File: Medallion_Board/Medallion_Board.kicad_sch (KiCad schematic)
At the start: 79 parts, among them J1 RYLR998, J2 EXPANSION, P1 JST_PH, P2 JST_BTN_1, P3 JST_BTN_2, P4 JST_BTN_3, P5 JST_EN, Q1 DMG3415U, SW1 KMR2, SW2 KMR2, U1 RT9080-33GJ5, U2 LC86LICMD, U3 ESP32-S3-MINI-1-N8, U4 BNO085, U5 MAX17048G_T10, U6 MCP73831T-2ACI_OT, X1 USB4085-GF-A

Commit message: migrating to nRF controller
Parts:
- removed C14, C18, C3: 1uF, Capacitor_SMD:C_0603_1608Metric, symbol Adafruit ESP32-S3 8MB No PSRAM-eagle-import:CAP_CERAMIC0603_NO
- removed C6: 10uF, Capacitor_SMD:C_0805_2012Metric, symbol Adafruit ESP32-S3 8MB No PSRAM-eagle-import:CAP_CERAMIC0805-NOOUTLINE
- removed C7: 0.1uF, Capacitor_SMD:C_0402_1005Metric, symbol Adafruit ESP32-S3 8MB No PSRAM-eagle-import:CAP_CERAMIC0805-NOOUTLINE
- removed C8: 47pF, Capacitor_SMD:C_0402_1005Metric, symbol Adafruit ESP32-S3 8MB No PSRAM-eagle-import:CAP_CERAMIC0805-NOOUTLINE
- removed FL1, FL2: BLM15EG121SN1D, BLM15EG121SN1D:BEADC1005X55N, symbol BLM15EG121SN1D:BLM15EG121SN1D
- removed J1: RYLR998, Connector_PinHeader_2.54mm:RYLR998, symbol Connector_Generic:Conn_01x05
- removed P5: JST_EN, S2B-PH-SM4-TB_LF__SN_:JST_S2B-PH-SM4-TB_LF__SN_, symbol S2B-PH-SM4-TB_LF__SN_:S2B-PH-SM4-TB_LF__SN_
- removed R2: 100K, Resistor_SMD:R_0603_1608Metric, symbol Adafruit ESP32-S3 8MB No PSRAM-eagle-import:RESISTOR_0603_NOOUT
- removed SW2: KMR2, Button_Switch_SMD:SW_Push_1P1T-SH_NO_CK_KMR2xxG, symbol Adafruit ESP32-S3 8MB No PSRAM-eagle-import:SWITCH_TACT_SMT4.6X2.8
- removed U3: ESP32-S3-MINI-1-N8, ESP32-S3-MINI-1-N8:XCVR_ESP32-S3-MINI-1-N8, symbol ESP32-S3-MINI-1-N8:ESP32-S3-MINI-1-N8
- added C3, C4: 10uF, Capacitor_SMD:C_0805_2012Metric, symbol Adafruit ESP32-S3 8MB No PSRAM-eagle-import:CAP_CERAMIC0805-NOOUTLINE
- added C6: 1uF, Capacitor_SMD:C_0603_1608Metric, symbol Adafruit ESP32-S3 8MB No PSRAM-eagle-import:CAP_CERAMIC0603_NO
- added L1: 10uH, LQM18DN100M70L:INDC1608X95N, symbol LQM18DN100M70L:LQM18DN100M70L
- added P1: JST_ONOFF, S2B-PH-SM4-TB_LF__SN_:JST_S2B-PH-SM4-TB_LF__SN_, symbol S2B-PH-SM4-TB_LF__SN_:S2B-PH-SM4-TB_LF__SN_
- added R1: 5.1K, Resistor_SMD:R_0603_1608Metric, symbol Adafruit ESP32-S3 8MB No PSRAM-eagle-import:RESISTOR_0603_NOOUT
- added R10, R11: 1K, Resistor_SMD:R_0603_1608Metric, symbol Adafruit ESP32-S3 8MB No PSRAM-eagle-import:RESISTOR_0603_NOOUT
- added R19, R21: 27R, Resistor_SMD:R_0603_1608Metric, symbol Adafruit ESP32-S3 8MB No PSRAM-eagle-import:RESISTOR_0603_NOOUT
- added U1: MDBT50Q-1MV2, MDBT50Q-1MV2:XCVR_MDBT50Q-1MV2, symbol MDBT50Q-1MV2:MDBT50Q-1MV2
- added Y1: 32.768KHZ, ABS07-32.768KHZ-7-T:XTAL_ABS07-32.768KHZ-7-T, symbol ABS07-32.768KHZ-7-T:ABS07-32.768KHZ-7-T
- C1, C2: value 10uF -> 12pF; footprint Capacitor_SMD:C_0805_2012Metric -> Capacitor_SMD:C_0402_1005Metric
- C8: renamed from C4; value KW-5R5C104-R -> 100mF
- D10, D11, D3, D4, D5, D6, D7, D8, D9: MPN (none) -> WS2812B-2020
- P2: renamed from P1; MPN (none) -> S2B-PH-SM4-TB(LF)(SN); PRICE (none) -> 0.37
- P3: renamed from P2; MPN (none) -> S2B-PH-SM4-TB(LF)(SN); PRICE (none) -> 0.37
- P4: MPN (none) -> S2B-PH-SM4-TB(LF)(SN); PRICE (none) -> 0.37
- P5: renamed from P3; MPN (none) -> S2B-PH-SM4-TB(LF)(SN); PRICE (none) -> 0.37
- R4: value 1Meg -> 100K
- R7: value 5.1K -> 5.6K
- renumbered C12 to C10, C10 to C11, C11 to C12, C21 to C13, C13 to C14, C22 to C15, C23 to C16, C24 to C17, C25 to C18, C26 to C19, C27 to C20, C28 to C21, C29 to C22, C30 to C23, C15 to C24, C17 to C25, C31 to C26, C16 to C27, C20 to C28, C19 to C7, J2 to J1, R8 to R12, R10 to R13, R16 to R14, R17 to R15, R9 to R16, R5 to R17, R6 to R18, R11 to R2, R13 to R20, R12 to R3, R1 to R5, R14 to R6, R15 to R8, R3 to R9, U5 to U2, U2 to U3, U1 to U4, U6 to U5, U4 to U6
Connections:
- net IO34_DBLTAP is gone; now on an unnamed net: R4.2
- net TXD0 is gone; now on an unnamed net: U3.1 (RXD)
- net 3.3V: now also R12.2, R13.2, R16.2, R2.2, R3.2, C4.1, R1.2, U1.30 (VDDH); no longer C1.1, C2.1, R7.2
- net BNO_NINT: now also U1.25 (P1.08)
- net BNO_NRST: now also U1.26 (P1.09/TRACEDATA3)
- net D+: now also R19.1, U1.35 (D+); no longer X1.A6 (DP1)
- net D-: now also R21.1, U1.34 (D-); no longer X1.B6 (DP2)
- net GND: now also C1.1, C2.1, R7.2, U6.10 (CLKSEL0), C3.2, C4.2, C6.2, P1.2, U1.1 (GND), U1.15 (GND), U1.2 (GND), U1.33 (GND), U1.55 (GND); no longer C1.2, C2.2, R4.1
- net GPS_ANT_ACTIVE: now also U1.7 (P1.14)
- net GPS_RESET: now also U1.8 (P1.15)
- net GPS_WAKEUP: now also U1.6 (P1.13)
- net LOW_BATT: now also U1.57 (P1.06)
- net NEOPIX: now also U1.58 (P1.07)
- net SCL: now also U1.16 (P0.27)
- net SDA: now also U1.19 (P0.26)
- net STATUS_LED: now also U1.59 (P1.05)
- net USER_BTN_1: now also U1.3 (P1.10)
- net USER_BTN_2: now also U1.4 (P1.11)
- net USER_BTN_3: now also U1.5 (P1.12)
- net VBUS: now also C5.1, U1.32 (VBUS)
- net VHI: now also R4.1
- net at U4.3 (EN): now also P1.1
- net OSC2: now reaches U6.26 (XOUT32/CLKSEL1)
- net OSC2: now also C2.2, U1.18 (P0.01/XL2), Y1.1
- net OSC1: now reaches U6.27 (XIN32)
- net OSC1: now also C1.2, U1.17 (P0.00/XL1), Y1.2
- removed net +3.3V: C5.1, R12.2, R13.2, R16.2, R2.2, R3.2
- net GPIO01 renamed GPIO19
- net GPIO19: now also U1.42 (P0.19)
- net GPIO02 renamed GPIO20
- net GPIO20: now also U1.44 (P0.20)
- net GPIO06 renamed GPIO21
- net GPIO21: now also U1.43 (P0.21)
- net GPIO11 renamed GPIO22
- net GPIO22: now also U1.46 (P0.22)
- net RESET: no longer names the net of R7.1
- net RESET: now also R10.2; no longer SW1.2
- net RXD0: no longer names the net of U3.2 (TXD)
- net RXD0: now also R11.1
- new net: C3.1, L1.2, U1.28 (VDD)
- new net: L1.1, U1.31 (DCCH)
- new net: R19.2, X1.A6 (DP1)
- new net: R21.2, X1.B6 (DP2)
- new net RXD_GPS: R11.2, U1.24 (P0.08)
- new net TXD_GPS: R10.1, U1.22 (P0.06)
- new net uC_RESET: C6.1, R1.1, SW1.2, U1.40 (P0.18/~{RESET})
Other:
- note added: "GNSS"
- note added: "LED"
- note added: "USB"
- note added: "nRF MODULE"
- note removed: "Bulk decoupling"
- note removed: "CONTROLLER"
- note removed: "GPS"
- note removed: "High-frequency filter"
- note removed: "I2C SUPPORT"
- note removed: "NEOPIXEL"
- note removed: "Place as near to ESP32 power rail as possible"
- note removed: "USB AND PROGRAMMING BUTTONS"
- moved on the sheet: C10, C11, C12, C13, C14, C15, C16, C17, C18, C19, C20, C21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

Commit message: Migrate to the nRF microcontroller. Attempt to implement my own lora section - will probably remove later.
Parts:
- added C28: 4.7uF, Capacitor_SMD:C_0603_1608Metric, symbol Adafruit ESP32-S3 8MB No PSRAM-eagle-import:CAP_CERAMIC0603_NO
- added C30, C31: NC, Capacitor_SMD:C_0603_1608Metric, symbol Adafruit ESP32-S3 8MB No PSRAM-eagle-import:CAP_CERAMIC0603_NO
- added IC1: 114993121, Wio-E5-LE:114993121, symbol 114993121:114993121
- added J2: RECE.20369.001E.01, RECE.20369:RECE20369001E01, symbol RECE_20369_001E_01:RECE.20369.001E.01
- added L2: 0R, LQM18DN100M70L:INDC1608X95N, symbol LQM18DN100M70L:LQM18DN100M70L
- added R17: 470R, Resistor_SMD:R_0603_1608Metric, symbol Adafruit ESP32-S3 8MB No PSRAM-eagle-import:RESISTOR_0603_NOOUT
- added R23: 5.6K, Resistor_SMD:R_0603_1608Metric, symbol Adafruit ESP32-S3 8MB No PSRAM-eagle-import:RESISTOR_0603_NOOUT
- added R24, R25: 22R, Resistor_SMD:R_0603_1608Metric, symbol Adafruit ESP32-S3 8MB No PSRAM-eagle-import:RESISTOR_0603_NOOUT
- added SW2: KMR2, Button_Switch_SMD:SW_Push_1P1T-SH_NO_CK_KMR2xxG, symbol Adafruit ESP32-S3 8MB No PSRAM-eagle-import:SWITCH_TACT_SMT4.6X2.8
- renumbered C28 to C29, R17 to R18, R18 to R19, R19 to R20, R20 to R21, R21 to R22
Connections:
- net 3.3V: now also C28.1, IC1.1 (VCC)
- net GND: now also C28.2, C30.2, C31.2, IC1.14 (GND_2), IC1.16 (GND_3), IC1.2 (GND_1), IC1.22 (GND_4), J2.1 (GND_1), J2.2 (GND_2), J2.3 (GND_3), R17.2, R23.2
- net RXD_LORA: now reaches U1.36 (P0.14)
- net RXD_LORA: now also R25.2
- net TXD_LORA: now reaches U1.37 (P0.13)
- net TXD_LORA: now also R24.1
- net LORA_RST: now reaches U1.56 (P1.04)
- net LORA_RST: now also IC1.17 (RST)
- new net: C30.1, IC1.15 (RFIO), L2.1
- new net: IC1.9 (PB7), R23.1, R24.2
- new net: IC1.10 (PB6), R25.1
- new net: IC1.24 (PB13), SW2.1
- new net: R17.1, SW2.2
- new net: C31.1, J2.4 (CENTRE), L2.2
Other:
- note added: "I need to figure out the values for the inductor and capacitors."
- title: (none) -> Off-grid People Tracking Puck

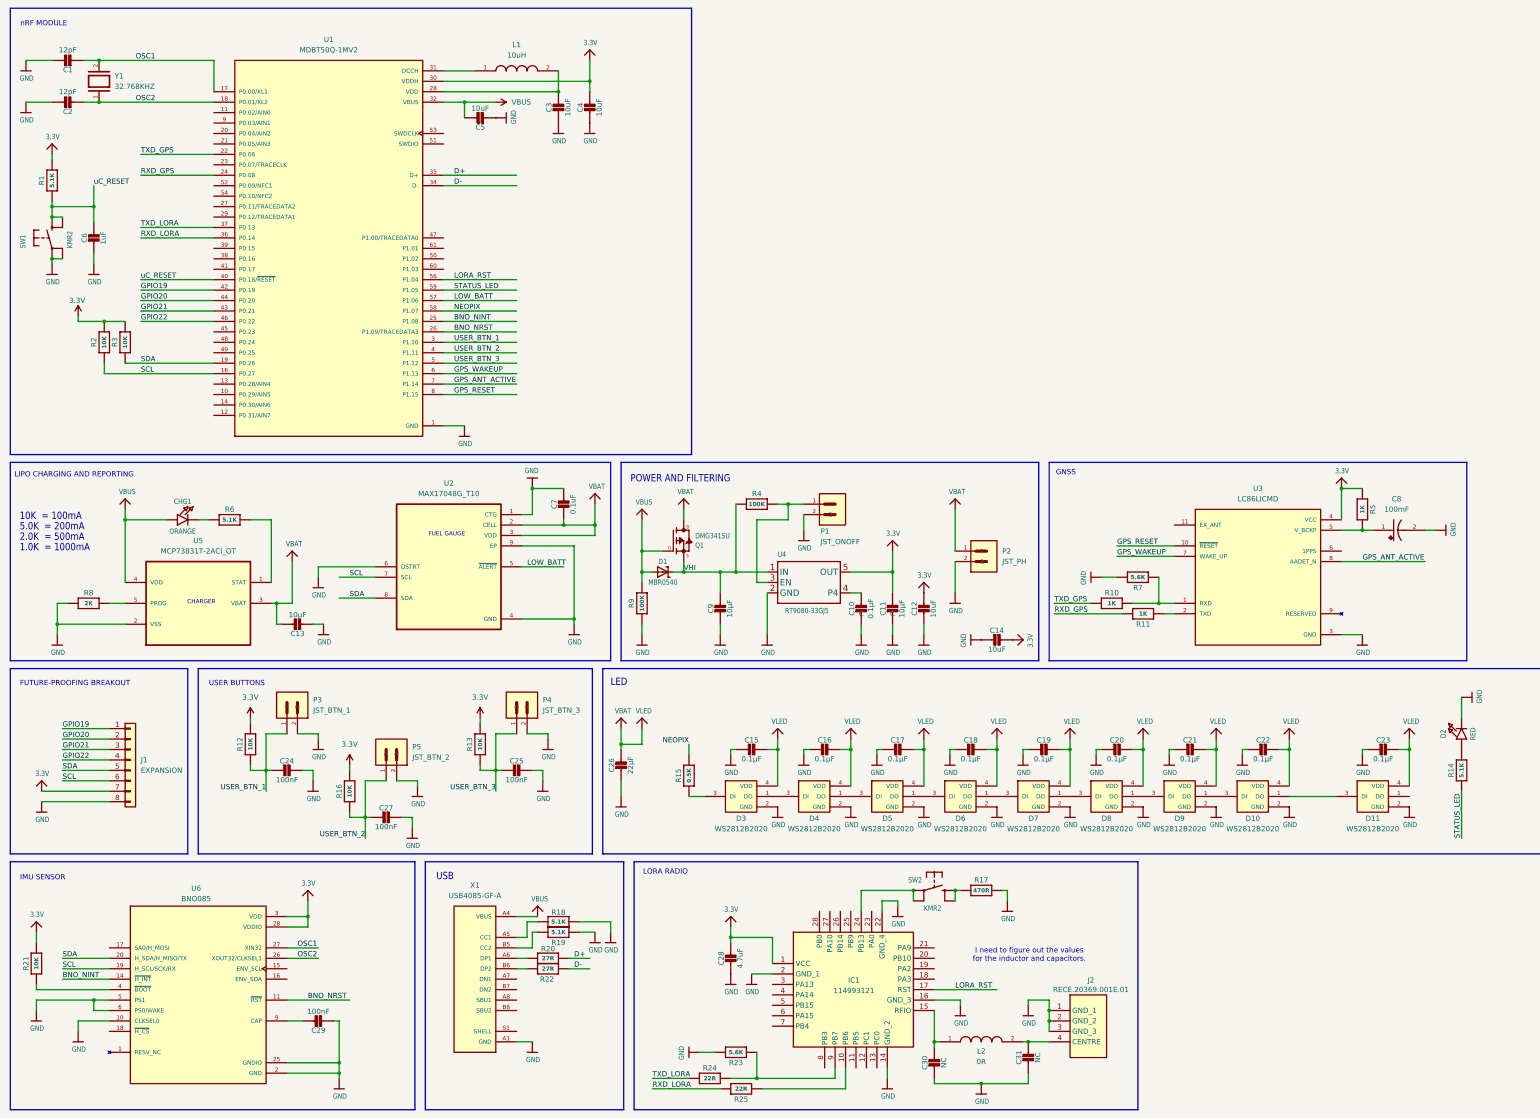
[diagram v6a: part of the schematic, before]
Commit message: Start PCB design again - compact requirements
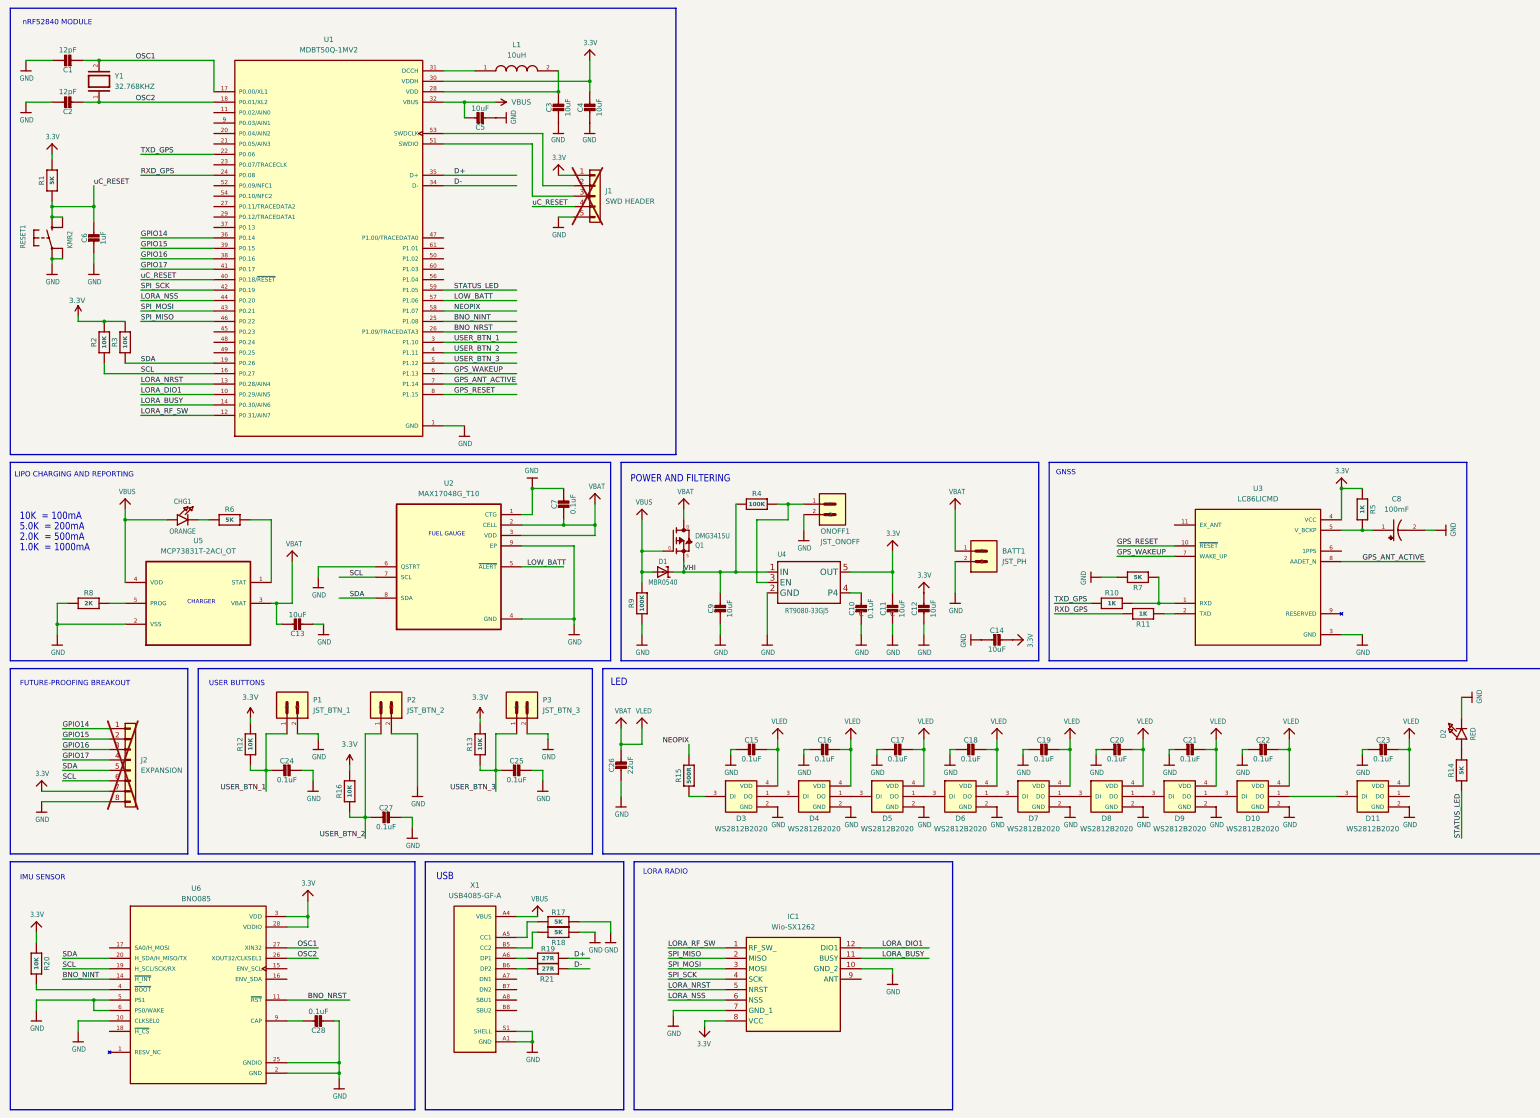
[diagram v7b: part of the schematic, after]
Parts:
- removed C28: 4.7uF, Capacitor_SMD:C_0603_1608Metric, symbol Adafruit ESP32-S3 8MB No PSRAM-eagle-import:CAP_CERAMIC0603_NO
- removed C30, C31: NC, Capacitor_SMD:C_0603_1608Metric, symbol Adafruit ESP32-S3 8MB No PSRAM-eagle-import:CAP_CERAMIC0603_NO
- removed IC1: 114993121, Wio-E5-LE:114993121, symbol 114993121:114993121
- removed J2: RECE.20369.001E.01, RECE.20369:RECE20369001E01, symbol RECE_20369_001E_01:RECE.20369.001E.01
- removed L2: 0R, LQM18DN100M70L:INDC1608X95N, symbol LQM18DN100M70L:LQM18DN100M70L
- removed R17: 470R, Resistor_SMD:R_0603_1608Metric, symbol Adafruit ESP32-S3 8MB No PSRAM-eagle-import:RESISTOR_0603_NOOUT
- removed R23: 5.6K, Resistor_SMD:R_0603_1608Metric, symbol Adafruit ESP32-S3 8MB No PSRAM-eagle-import:RESISTOR_0603_NOOUT
- removed R24, R25: 22R, Resistor_SMD:R_0603_1608Metric, symbol Adafruit ESP32-S3 8MB No PSRAM-eagle-import:RESISTOR_0603_NOOUT
- removed SW2: KMR2, Button_Switch_SMD:SW_Push_1P1T-SH_NO_CK_KMR2xxG, symbol Adafruit ESP32-S3 8MB No PSRAM-eagle-import:SWITCH_TACT_SMT4.6X2.8
- added IC1: Wio-SX1262, 114993390:114993390, symbol 114993390:114993390
- added J1: SWD HEADER, Connector_PinHeader_2.54mm:PinHeader_1x05_P2.54mm_Vertical, symbol Connector_Generic:Conn_01x05
- C1, C2: MPN (none) -> GMC04CG120J6R3NT
- C10: value 0.1µF -> 0.1uF; MPN (none) -> 0402B104K160HI
- C11, C13, C9: value 10µF -> 10uF; MPN (none) -> 0805W106K6R3CC
- C12, C14, C3, C4, C5: MPN (none) -> 0805W106K6R3CC
- C15, C16, C17, C18, C19, C20, C21, C22, C23: value 0.1µF -> 0.1uF; footprint Capacitor_SMD:C_0603_1608Metric -> Capacitor_SMD:C_0402_1005Metric; MPN (none) -> 0402B104K160HI
- C24, C25, C27: value 100nF -> 0.1uF; footprint Capacitor_SMD:C_0603_1608Metric -> Capacitor_SMD:C_0402_1005Metric; MPN (none) -> 0402B104K160HI
- C26: value 22µF -> 22uF; footprint Capacitor_SMD:C_0805_2012Metric -> Capacitor_SMD:C_0402_1005Metric; MPN (none) -> GRM155R61A224KE19D
- C28: renamed from C29; value 100nF -> 0.1uF; footprint Capacitor_SMD:C_0603_1608Metric -> Capacitor_SMD:C_0402_1005Metric; MPN (none) -> 0402B104K160HI
- C6: MPN (none) -> 0603B105K100XD
- C7: MPN (none) -> 0402B104K160HI
- C8: MANUFACTURER Seiko -> (none); MF Seiko Instruments -> (none); MP XH414HG-IV01E -> (none)
- CHG1: footprint LED_SMD:LED_0805_2012Metric -> LED_SMD:LED_0603_1608Metric
- J2: renamed from J1; now not fitted
- R1, R14, R6: value 5.1K -> 5K; MPN (none) -> RT0603BRE075KL
- R10, R11, R5: MPN (none) -> RC0603FR-071KL
- R12, R13, R16, R2, R3: MPN (none) -> RC0603FR-0710KL
- R15: value 0.5K -> 500R; MPN (none) -> RT0603BRC07500RL
- R17: renamed from R18; value 5.1K -> 5K; MPN (none) -> RT0603BRE075KL
- R18: renamed from R19; value 5.1K -> 5K; MPN (none) -> RT0603BRE075KL
- R19: renamed from R20; MPN (none) -> RC0603FR-0727RL
- R20: renamed from R21; MPN (none) -> RC0603FR-0710KL
- R21: renamed from R22; MPN (none) -> RC0603FR-0727RL
- R4, R9: MPN (none) -> RC0603FR-07100KL
- R7: value 5.6K -> 5K; MPN (none) -> RT0603BRE075KL
- R8: MPN (none) -> RC0603FR-072KL
- renumbered P2 to BATT1, P1 to ONOFF1, P3 to P1, P5 to P2, P4 to P3, SW1 to RESET1
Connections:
- net RXD_LORA is gone; now on net GPIO14: U1.36 (P0.14)
- net 3.3V: now also IC1.8 (VCC), J1.1 (VCC)
- net GND: now also X1.S1 (SHELL), X1.S2 (SHELL), X1.S3 (SHELL), X1.S4 (SHELL), IC1.10 (GND_2), IC1.7 (GND_1), J1.5 (GND)
- net uC_RESET: now also J1.4 (RST)
- net LORA_DIO1: now reaches U1.10 (P0.29/AIN5)
- net LORA_DIO1: now also IC1.12 (DIO1)
- net LORA_RF_SW: now reaches U1.12 (P0.31/AIN7)
- net LORA_RF_SW: now also IC1.1 (RF_SW_)
- net LORA_NRST: now reaches U1.13 (P0.28/AIN4)
- net LORA_NRST: now also IC1.5 (NRST)
- net LORA_BUSY: now reaches U1.14 (P0.30/AIN6)
- net LORA_BUSY: now also IC1.11 (BUSY)
- net GPIO16: now reaches U1.38 (P0.16)
- net GPIO16: now also J2.3 (Pin_3)
- net GPIO15: now reaches U1.39 (P0.15)
- net GPIO15: now also J2.2 (Pin_2)
- net GPIO17: now reaches U1.41 (P0.17)
- net GPIO17: now also J2.4 (Pin_4)
- net at U1.51 (SWDIO): now also J1.3 (SWDIO)
- net at U1.53 (SWDCLK): now also J1.2 (SWDCLK)
- net GPIO19 renamed GPIO14
- net GPIO14: no longer U1.42 (P0.19)
- net GPIO20 renamed LORA_NSS
- net LORA_NSS: now also IC1.6 (NSS); no longer J2.2 (Pin_2)
- net GPIO21 renamed SPI_MOSI
- net SPI_MOSI: now also IC1.3 (MOSI); no longer J2.3 (Pin_3)
- net GPIO22 renamed SPI_MISO
- net SPI_MISO: now also IC1.2 (MISO); no longer J2.4 (Pin_4)
- net LORA_RST: no longer names the net of U1.56 (P1.04)
- net TXD_LORA: no longer names the net of U1.37 (P0.13)
- new net SPI_SCK: IC1.4 (SCK), U1.42 (P0.19)
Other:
- note added: "nRF52840 MODULE"
- note removed: "I need to figure out the values for the inductor and capacitors."
- note removed: "nRF MODULE"
- moved on the sheet: P2, R20
